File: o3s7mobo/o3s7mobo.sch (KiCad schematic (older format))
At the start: 2 parts

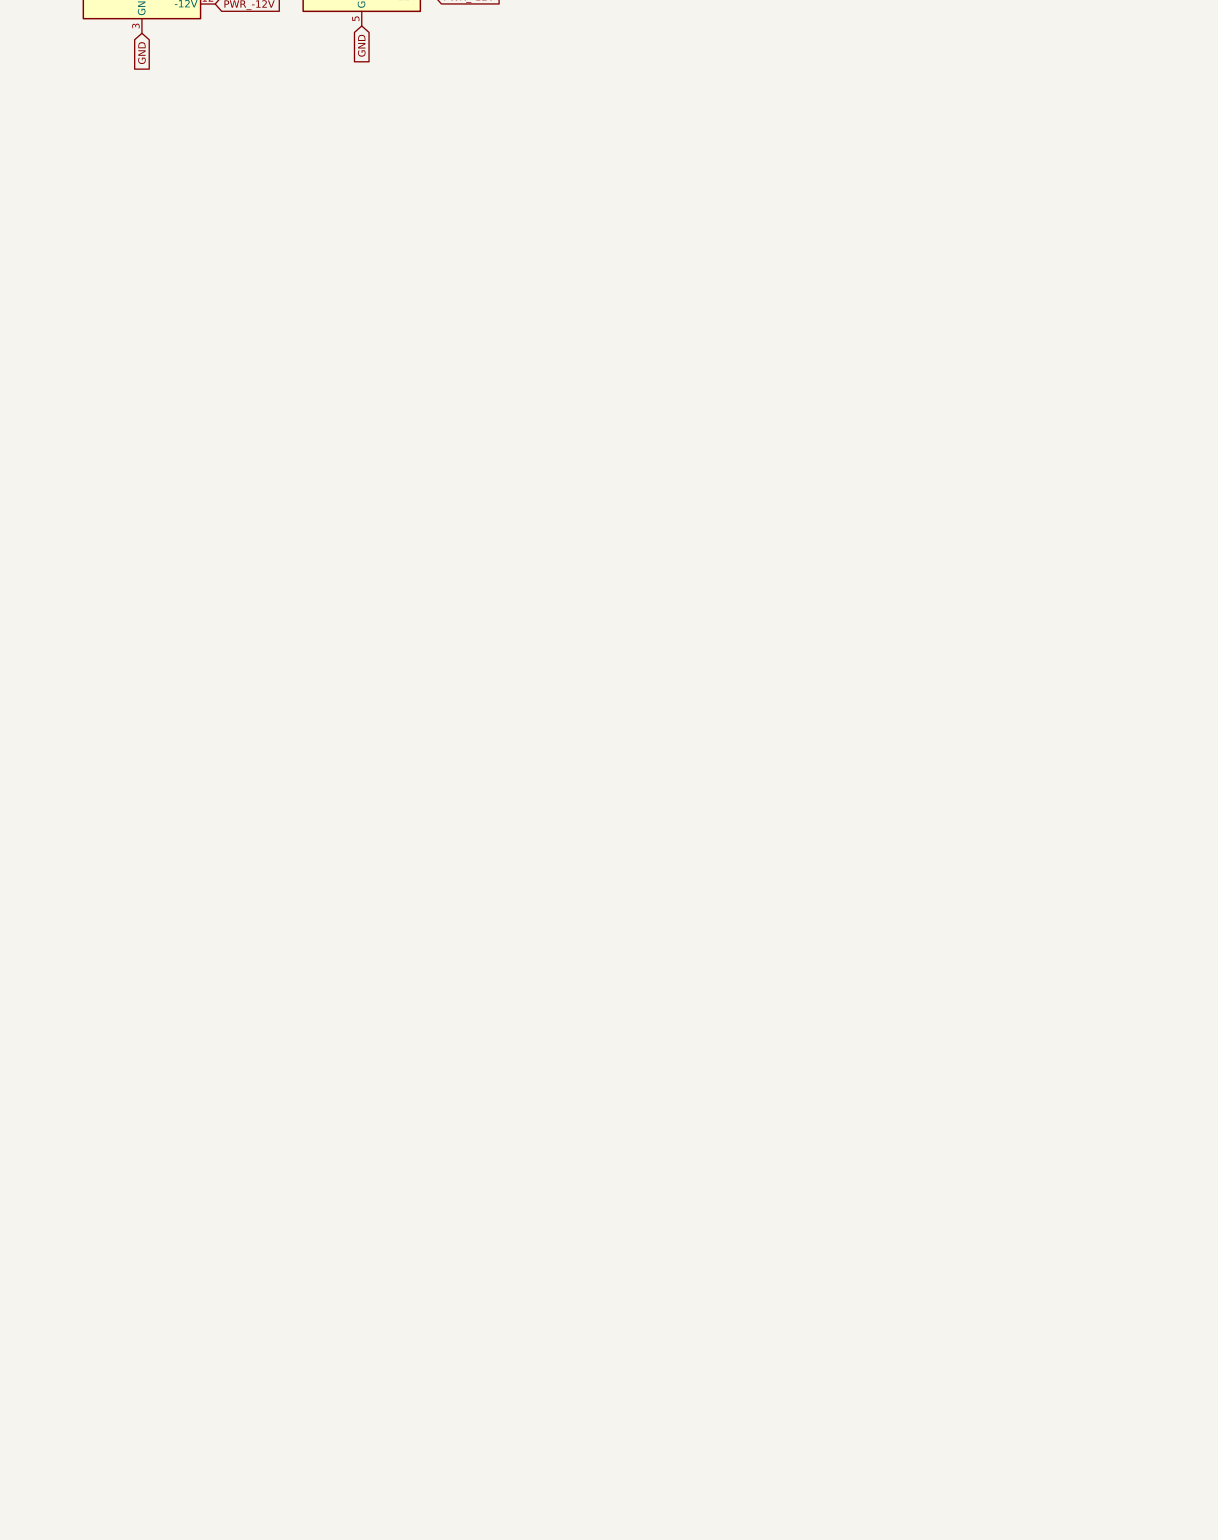
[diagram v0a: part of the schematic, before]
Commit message: Added Socket 7 schematics
I'm willing to have these schematics uploaded to the official KiCAD repositories; I'm just unsure how.
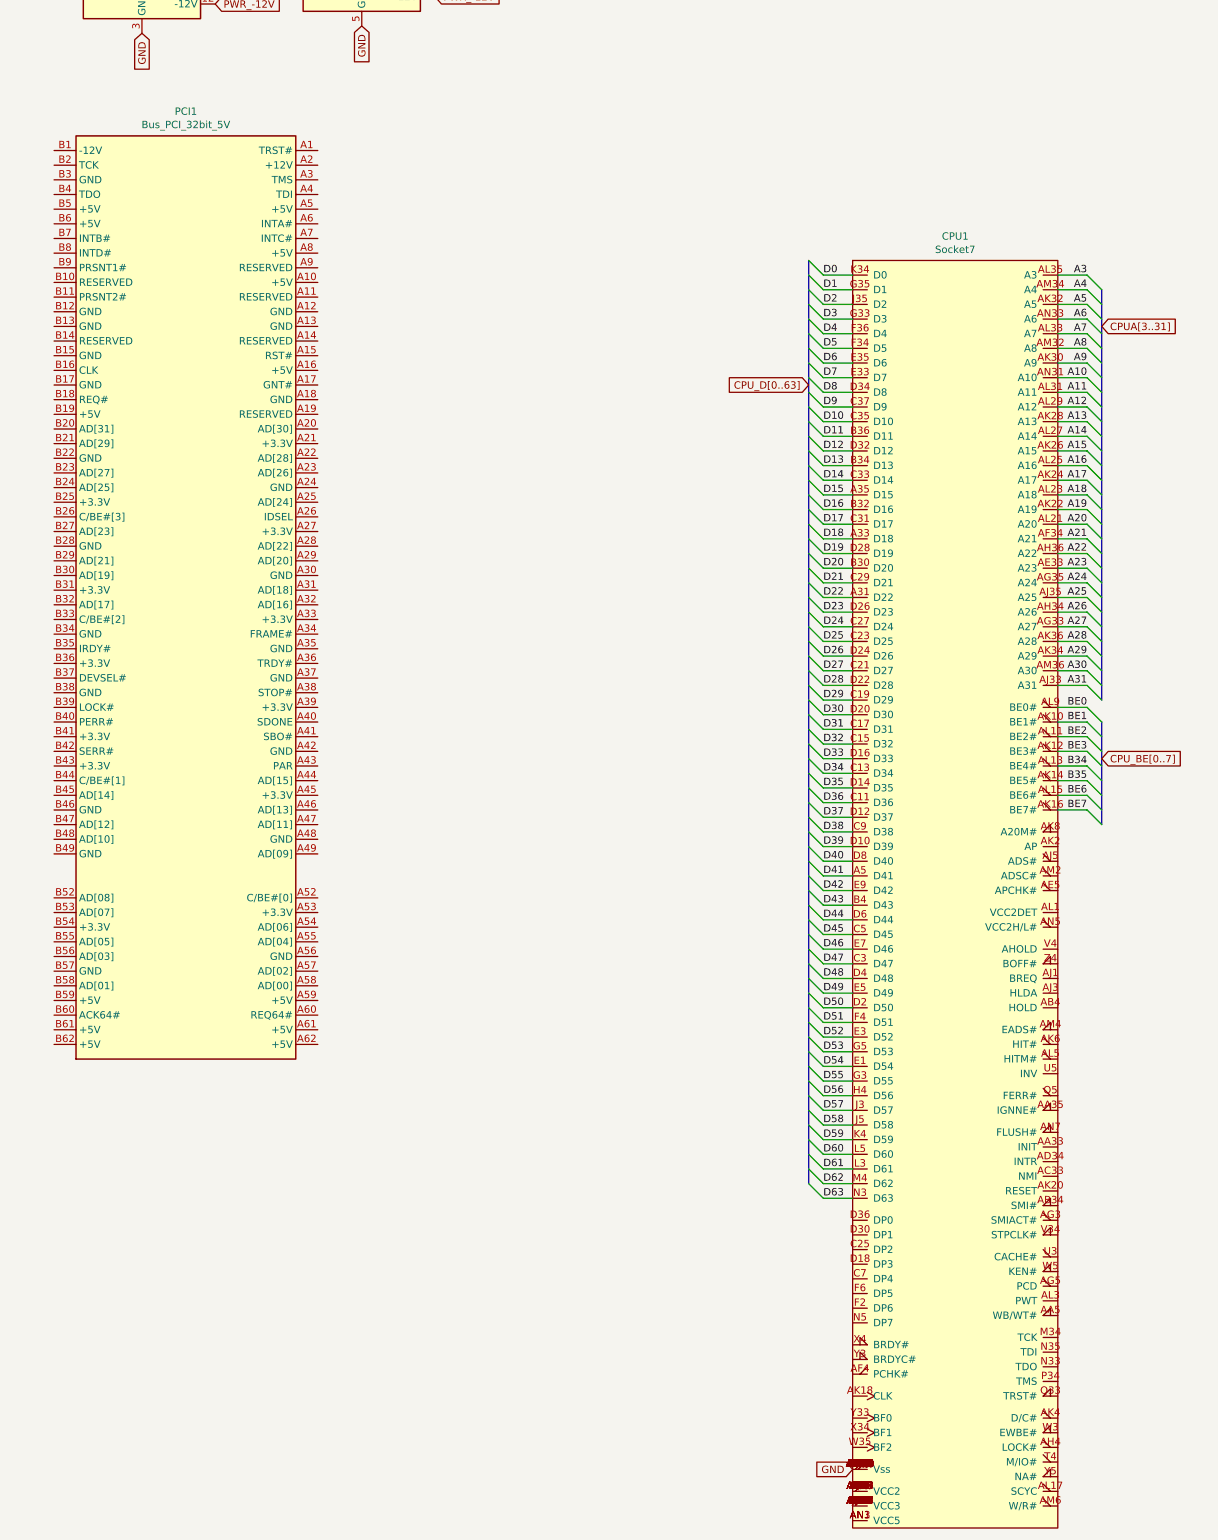
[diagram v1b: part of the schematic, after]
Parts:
- added CPU1: Socket7, Downloaded:Socket_7, symbol Downloaded:Socket7
- added PCI1: Bus_PCI_32bit_5V, symbol Connector:Bus_PCI_32bit_5V
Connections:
- net GND: now also CPU1.A3 (Vss), CPU1.AB2 (Vss), CPU1.AB36 (Vss), CPU1.AD2 (Vss), CPU1.AD36 (Vss), CPU1.AF2 (Vss), CPU1.AF36 (Vss), CPU1.AH2 (Vss), CPU1.AJ17 (Vss), CPU1.AJ21 (Vss), CPU1.AJ25 (Vss), CPU1.AJ27 (Vss), CPU1.AJ31 (Vss), CPU1.AJ37 (Vss), CPU1.AJ7 (Vss), CPU1.AJ9 (Vss), CPU1.AL37 (Vss), CPU1.AM10 (Vss), CPU1.AM12 (Vss), CPU1.AM14 (Vss), CPU1.AM16 (Vss), CPU1.AM18 (Vss), CPU1.AM20 (Vss), CPU1.AM22 (Vss), CPU1.AM24 (Vss), CPU1.AM26 (Vss), CPU1.AM28 (Vss), CPU1.AM30 (Vss), CPU1.AM8 (Vss), CPU1.AN37 (Vss), CPU1.B10 (Vss), CPU1.B12 (Vss), CPU1.B14 (Vss), CPU1.B16 (Vss), CPU1.B18 (Vss), CPU1.B20 (Vss), CPU1.B22 (Vss), CPU1.B24 (Vss), CPU1.B26 (Vss), CPU1.B28 (Vss), CPU1.B6 (Vss), CPU1.B8 (Vss), CPU1.E11 (Vss), CPU1.E13 (Vss), CPU1.E19 (Vss), CPU1.E23 (Vss), CPU1.E29 (Vss), CPU1.E31 (Vss), CPU1.H2 (Vss), CPU1.H36 (Vss), CPU1.K2 (Vss), CPU1.K36 (Vss), CPU1.M2 (Vss), CPU1.M36 (Vss), CPU1.P2 (Vss), CPU1.P36 (Vss), CPU1.R2 (Vss), CPU1.R36 (Vss), CPU1.T2 (Vss), CPU1.T36 (Vss), CPU1.U35 (Vss), CPU1.V2 (Vss), CPU1.V36 (Vss), CPU1.X2 (Vss), CPU1.X36 (Vss), CPU1.Z2 (Vss), CPU1.Z36 (Vss)
- new net: CPU1.A11 (VCC2), CPU1.A13 (VCC2), CPU1.A15 (VCC2), CPU1.A17 (VCC2), CPU1.A7 (VCC2), CPU1.A9 (VCC2), CPU1.AA1 (VCC2), CPU1.AC1 (VCC2), CPU1.AE1 (VCC2), CPU1.AG1 (VCC2), CPU1.AJ11 (VCC2), CPU1.AN11 (VCC2), CPU1.AN13 (VCC2), CPU1.AN15 (VCC2), CPU1.AN17 (VCC2), CPU1.AN19 (VCC2), CPU1.AN9 (VCC2), CPU1.B2 (VCC2), CPU1.E15 (VCC2), CPU1.G1 (VCC2), CPU1.J1 (VCC2), CPU1.L1 (VCC2), CPU1.N1 (VCC2), CPU1.Q1 (VCC2), CPU1.S1 (VCC2), CPU1.U1 (VCC2), CPU1.W1 (VCC2), CPU1.Y1 (VCC2)
- new net: CPU1.A19 (VCC3), CPU1.A21 (VCC3), CPU1.A23 (VCC3), CPU1.A25 (VCC3), CPU1.A27 (VCC3), CPU1.A29 (VCC3), CPU1.AA37 (VCC3), CPU1.AC37 (VCC3), CPU1.AE37 (VCC3), CPU1.AG37 (VCC3), CPU1.AJ19 (VCC3), CPU1.AJ29 (VCC3), CPU1.AN21 (VCC3), CPU1.AN23 (VCC3), CPU1.AN25 (VCC3), CPU1.AN27 (VCC3), CPU1.AN29 (VCC3), CPU1.E21 (VCC3), CPU1.E27 (VCC3), CPU1.E37 (VCC3), CPU1.G37 (VCC3), CPU1.J37 (VCC3), CPU1.L33 (VCC3), CPU1.L37 (VCC3), CPU1.N37 (VCC3), CPU1.Q37 (VCC3), CPU1.S37 (VCC3), CPU1.T34 (VCC3), CPU1.U33 (VCC3), CPU1.U37 (VCC3), CPU1.W37 (VCC3), CPU1.Y37 (VCC3)
- new net: CPU1.AN1 (VCC5), CPU1.AN3 (VCC5)
- new net A10: CPU1.AN31 (A10)
- new net A11: CPU1.AL31 (A11)
- new net A12: CPU1.AL29 (A12)
- new net A13: CPU1.AK28 (A13)
- new net A14: CPU1.AL27 (A14)
- new net A15: CPU1.AK26 (A15)
- new net A16: CPU1.AL25 (A16)
- new net A17: CPU1.AK24 (A17)
- new net A18: CPU1.AL23 (A18)
- new net A19: CPU1.AK22 (A19)
- new net A20: CPU1.AL21 (A20)
- new net A21: CPU1.AF34 (A21)
- new net A22: CPU1.AH36 (A22)
- new net A23: CPU1.AE33 (A23)
- new net A24: CPU1.AG35 (A24)
- new net A25: CPU1.AJ35 (A25)
- new net A26: CPU1.AH34 (A26)
- new net A27: CPU1.AG33 (A27)
- new net A28: CPU1.AK36 (A28)
- new net A29: CPU1.AK34 (A29)
- new net A3: CPU1.AL35 (A3)
- new net A30: CPU1.AM36 (A30)
- new net A31: CPU1.AJ33 (A31)
- new net A4: CPU1.AM34 (A4)
- new net A5: CPU1.AK32 (A5)
- new net A6: CPU1.AN33 (A6)
- new net A7: CPU1.AL33 (A7)
- new net A8: CPU1.AM32 (A8)
- new net A9: CPU1.AK30 (A9)
- new net B34: CPU1.AL13 (BE4#)
- new net B35: CPU1.AK14 (BE5#)
- new net BE0: CPU1.AL9 (BE0#)
- new net BE1: CPU1.AK10 (BE1#)
- new net BE2: CPU1.AL11 (BE2#)
- new net BE3: CPU1.AK12 (BE3#)
- new net BE6: CPU1.AL15 (BE6#)
- new net BE7: CPU1.AK16 (BE7#)
- new net D0: CPU1.K34 (D0)
- new net D1: CPU1.G35 (D1)
- new net D10: CPU1.C35 (D10)
- new net D11: CPU1.B36 (D11)
- new net D12: CPU1.D32 (D12)
- new net D13: CPU1.B34 (D13)
- new net D14: CPU1.C33 (D14)
- new net D15: CPU1.A35 (D15)
- new net D16: CPU1.B32 (D16)
- new net D17: CPU1.C31 (D17)
- new net D18: CPU1.A33 (D18)
- new net D19: CPU1.D28 (D19)
- new net D2: CPU1.J35 (D2)
- new net D20: CPU1.B30 (D20)
- new net D21: CPU1.C29 (D21)
- new net D22: CPU1.A31 (D22)
- new net D23: CPU1.D26 (D23)
- new net D24: CPU1.C27 (D24)
- new net D25: CPU1.C23 (D25)
- new net D26: CPU1.D24 (D26)
- new net D27: CPU1.C21 (D27)
- new net D28: CPU1.D22 (D28)
- new net D29: CPU1.C19 (D29)
- new net D3: CPU1.G33 (D3)
- new net D30: CPU1.D20 (D30)
- new net D31: CPU1.C17 (D31)
- new net D32: CPU1.C15 (D32)
- new net D33: CPU1.D16 (D33)
- new net D34: CPU1.C13 (D34)
- new net D35: CPU1.D14 (D35)
- new net D36: CPU1.C11 (D36)
- new net D37: CPU1.D12 (D37)
- new net D38: CPU1.C9 (D38)
- new net D39: CPU1.D10 (D39)
- new net D4: CPU1.F36 (D4)
- new net D40: CPU1.D8 (D40)
- new net D41: CPU1.A5 (D41)
- new net D42: CPU1.E9 (D42)
- new net D43: CPU1.B4 (D43)
- new net D44: CPU1.D6 (D44)
- new net D45: CPU1.C5 (D45)
- new net D46: CPU1.E7 (D46)
- new net D47: CPU1.C3 (D47)
- new net D48: CPU1.D4 (D48)
- new net D49: CPU1.E5 (D49)
- new net D5: CPU1.F34 (D5)
- new net D50: CPU1.D2 (D50)
- new net D51: CPU1.F4 (D51)
- new net D52: CPU1.E3 (D52)
- new net D53: CPU1.G5 (D53)
- new net D54: CPU1.E1 (D54)
- new net D55: CPU1.G3 (D55)
- new net D56: CPU1.H4 (D56)
- new net D57: CPU1.J3 (D57)
- new net D58: CPU1.J5 (D58)
- new net D59: CPU1.K4 (D59)
- new net D6: CPU1.E35 (D6)
- new net D60: CPU1.L5 (D60)
- new net D61: CPU1.L3 (D61)
- new net D62: CPU1.M4 (D62)
- new net D63: CPU1.N3 (D63)
- new net D7: CPU1.E33 (D7)
- new net D8: CPU1.D34 (D8)
- new net D9: CPU1.C37 (D9)

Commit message: Been too long
Forgot I never pushed this.
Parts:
- added NB1: M1542, Downloaded:M1541, symbol Downloaded:M1542
- added PCI2, PCI3, PCI4: Bus_PCI_32bit_5V, Downloaded:PCI, symbol Connector:Bus_PCI_32bit_5V
- PCI1: footprint (none) -> Downloaded:PCI
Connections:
- new net BEJ0: NB1.AF13 (BEJ0)
- new net BEJ1: NB1.AE13 (BEJ1)
- new net BEJ2: NB1.AD13 (BEJ2)
- new net BEJ3: NB1.AC13 (BEJ3)
- new net BEJ4: NB1.AB13 (BEJ4)
- new net BEJ5: NB1.AF12 (BEJ5)
- new net BEJ6: NB1.AE12 (BEJ6)
- new net BEJ7: NB1.AD12 (BEJ7)
- new net HA10: NB1.P3 (HA10)
- new net HA11: NB1.P2 (HA11)
- new net HA12: NB1.P1 (HA12)
- new net HA13: NB1.R5 (HA13)
- new net HA14: NB1.R4 (HA14)
- new net HA15: NB1.R3 (HA15)
- new net HA16: NB1.R2 (HA16)
- new net HA17: NB1.R1 (HA17)
- new net HA18: NB1.T4 (HA18)
- new net HA19: NB1.M1 (HA19)
- new net HA20: NB1.M2 (HA20)
- new net HA21: NB1.M3 (HA21)
- new net HA22: NB1.M4 (HA22)
- new net HA23: NB1.M5 (HA23)
- new net HA24: NB1.L1 (HA24)
- new net HA25: NB1.L2 (HA25)
- new net HA26: NB1.L3 (HA26)
- new net HA27: NB1.K1 (HA27)
- new net HA28: NB1.K2 (HA28)
- new net HA29: NB1.K3 (HA29)
- new net HA3: NB1.N5 (HA3)
- new net HA30: NB1.J1 (HA30)
- new net HA31: NB1.H1 (HA31)
- new net HA4: NB1.N4 (HA4)
- new net HA5: NB1.N3 (HA5)
- new net HA6: NB1.N2 (HA6)
- new net HA7: NB1.N1 (HA7)
- new net HA8: NB1.P5 (HA8)
- new net HA9: NB1.P4 (HA9)
- new net HD0: NB1.T3 (HD0)
- new net HD1: NB1.T2 (HD1)
- new net HD10: NB1.V3 (HD10)
- new net HD11: NB1.V2 (HD11)
- new net HD12: NB1.V1 (HD12)
- new net HD13: NB1.W5 (HD13)
- new net HD14: NB1.W4 (HD14)
- new net HD15: NB1.W3 (HD15)
- new net HD16: NB1.W2 (HD16)
- new net HD17: NB1.W1 (HD17)
- new net HD18: NB1.Y4 (HD18)
- new net HD19: NB1.Y3 (HD19)
- new net HD2: NB1.T1 (HD2)
- new net HD20: NB1.Y2 (HD20)
- new net HD21: NB1.Y1 (HD21)
- new net HD22: NB1.AA3 (HD22)
- new net HD23: NB1.AA2 (HD23)
- new net HD24: NB1.AA1 (HD24)
- new net HD25: NB1.AA4 (HD25)
- new net HD26: NB1.AB2 (HD26)
- new net HD27: NB1.AB1 (HD27)
- new net HD28: NB1.AB3 (HD28)
- new net HD29: NB1.AB4 (HD29)
- new net HD3: NB1.U5 (HD3)
- new net HD30: NB1.AC1 (HD30)
- new net HD31: NB1.AC2 (HD31)
- new net HD32: NB1.AC3 (HD32)
- new net HD33: NB1.AD1 (HD33)
- new net HD34: NB1.AE1 (HD34)
- new net HD35: NB1.AF1 (HD35)
- new net HD36: NB1.AD2 (HD36)
- new net HD37: NB1.AF2 (HD37)
- new net HD38: NB1.AD3 (HD38)
- new net HD39: NB1.AE3 (HD39)
- new net HD4: NB1.U4 (HD4)
- new net HD40: NB1.AF3 (HD40)
- new net HD41: NB1.AD4 (HD41)
- new net HD42: NB1.AE4 (HD42)
- new net HD43: NB1.AF4 (HD43)
- new net HD44: NB1.AD5 (HD44)
- new net HD45: NB1.AE5 (HD45)
- new net HD46: NB1.AF5 (HD46)
- new net HD47: NB1.AC6 (HD47)
- new net HD48: NB1.AD6 (HD48)
- new net HD49: NB1.AE6 (HD49)
- new net HD5: NB1.U3 (HD5)
- new net HD50: NB1.AF6 (HD50)
- new net HD51: NB1.AC7 (HD51)
- new net HD52: NB1.AD7 (HD52)
- new net HD53: NB1.AE7 (HD53)
- new net HD54: NB1.AF7 (HD54)
- new net HD55: NB1.AB8 (HD55)
- new net HD56: NB1.AC8 (HD56)
- new net HD57: NB1.AD8 (HD57)
- new net HD58: NB1.AE8 (HD58)
- new net HD59: NB1.AF8 (HD59)
- new net HD6: NB1.U2 (HD6)
- new net HD60: NB1.AB9 (HD60)
- new net HD61: NB1.AC9 (HD61)
- new net HD62: NB1.AD9 (HD62)
- new net HD63: NB1.AE9 (HD63)
- new net HD7: NB1.U1 (HD7)
- new net HD8: NB1.V5 (HD8)
- new net HD9: NB1.V4 (HD9)
